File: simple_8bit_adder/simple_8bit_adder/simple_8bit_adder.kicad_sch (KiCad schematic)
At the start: 46 parts, among them Q10_0 2N7002, Q10_1 2N7002, Q11_0 2N7002, Q15_0 2N7002, Q15_1 2N7002, Q15_2 2N7002, Q15_3 2N7002, Q19_0 2N7002, Q19_1 2N7002, Q1_0 2N7002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

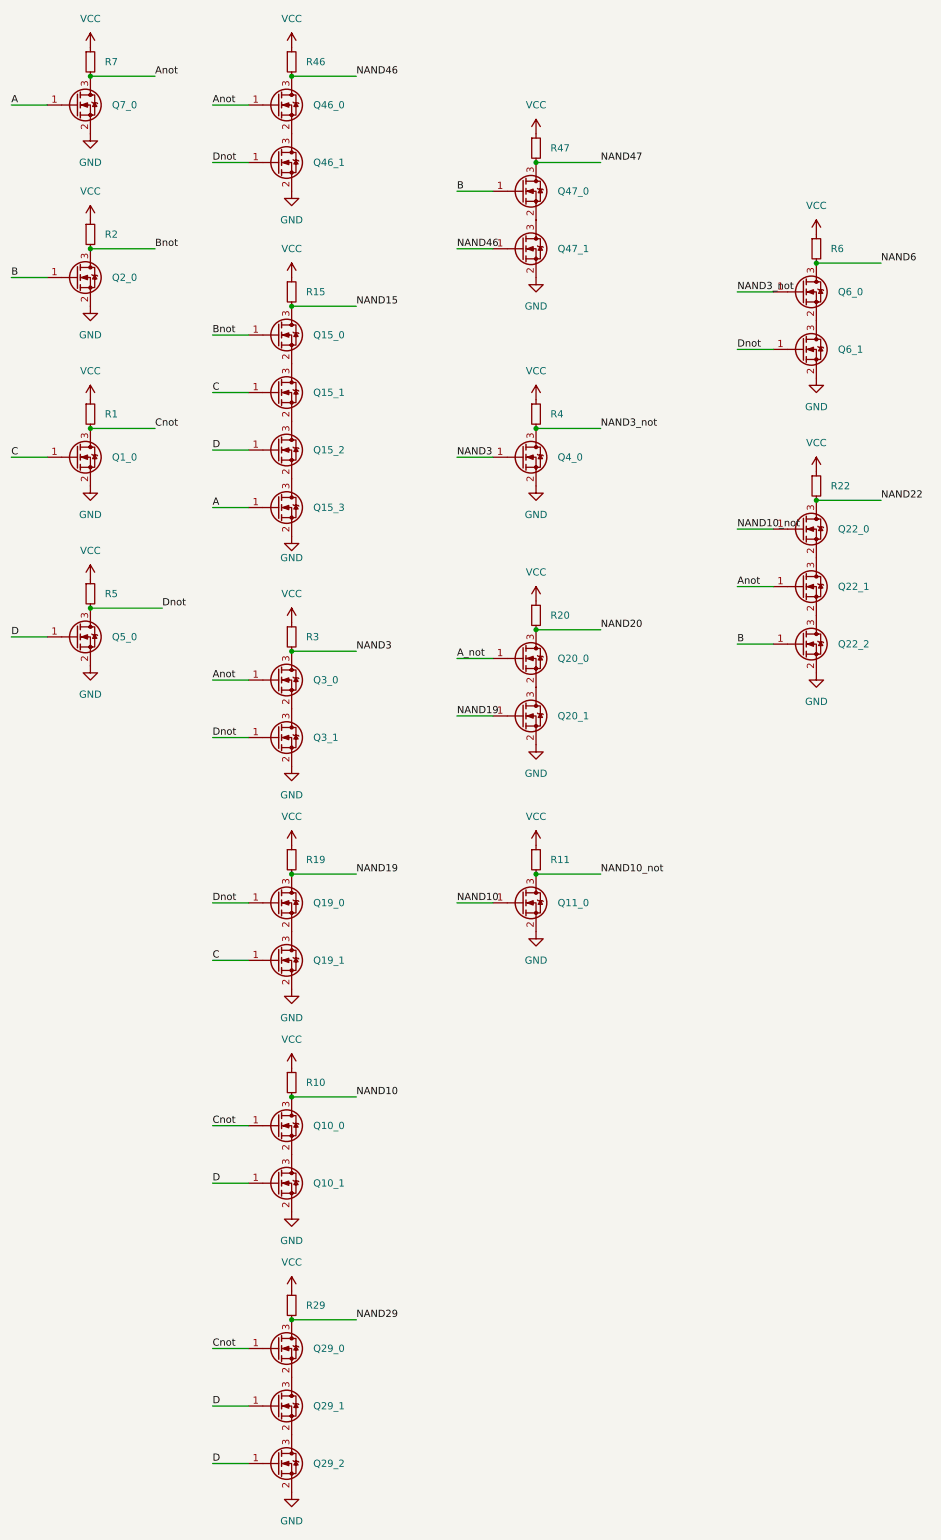
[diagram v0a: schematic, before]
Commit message: added example files
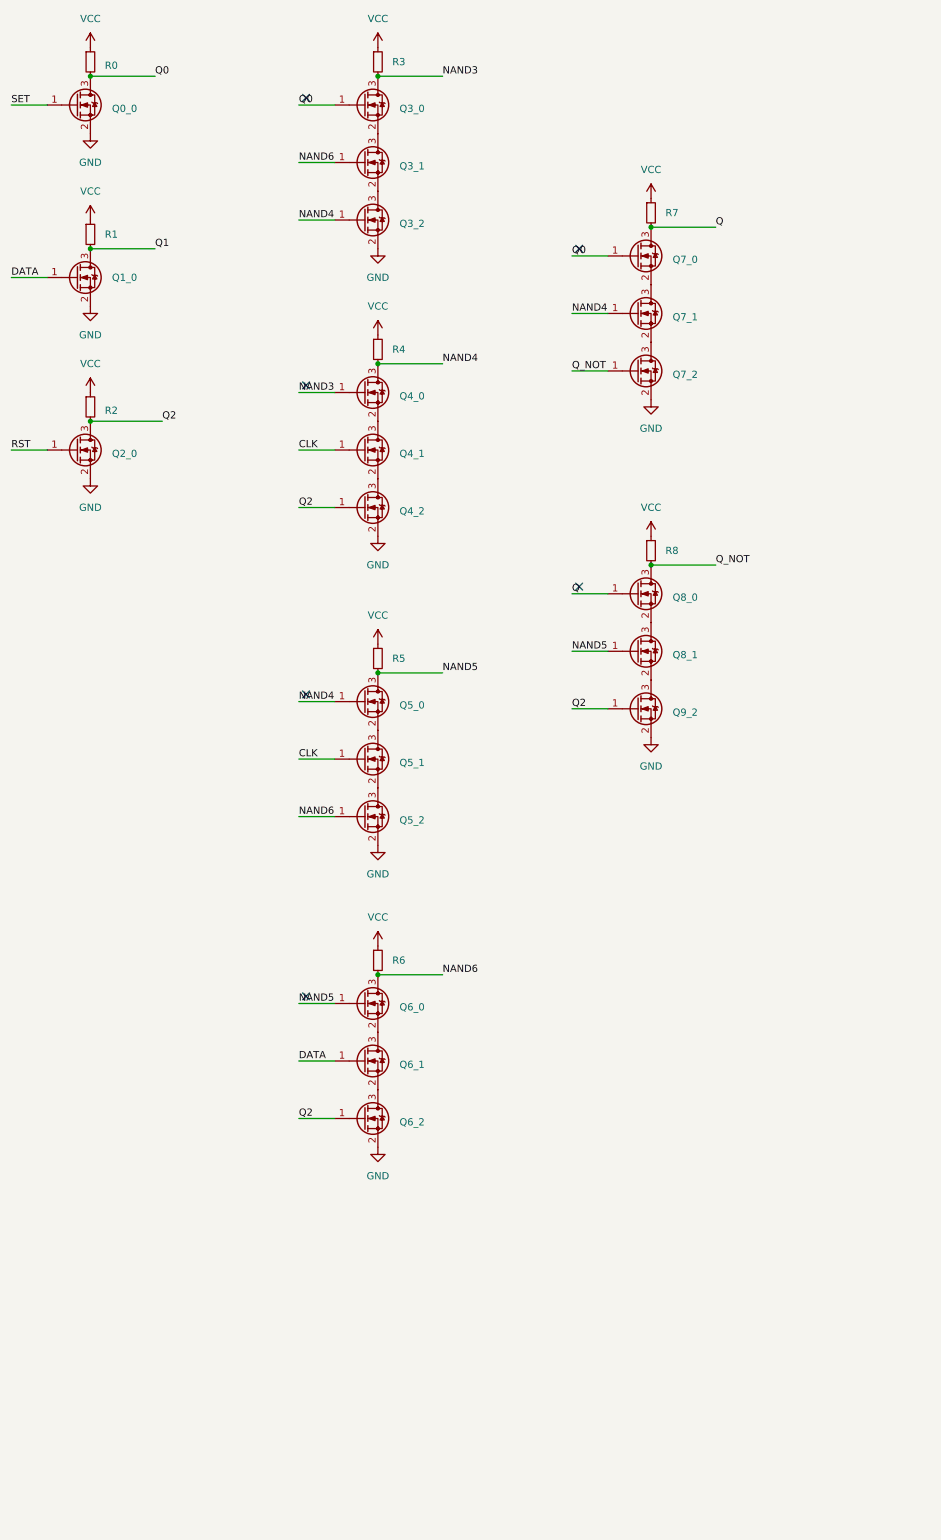
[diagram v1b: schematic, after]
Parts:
- removed Q10_0, Q10_1, Q11_0, Q15_0, Q15_1, Q15_2, Q15_3, Q19_0, Q19_1, Q20_0, Q20_1, Q22_0, Q22_1, Q22_2, Q29_0, Q29_1, Q29_2, Q2_0, Q46_0, Q46_1, Q47_0, Q47_1: 2N7002, Package_TO_SOT_SMD:SOT-23, symbol Transistor_FET:2N7002
- removed R10, R11, R15, R19, R2, R20, R22, R29, R46, R47: R_Small, Resistor_SMD:R_0402_1005Metric, symbol Device:R_Small
- added Q3_2, Q4_1, Q4_2, Q5_0, Q5_1, Q5_2, Q6_2, Q7_0, Q7_1, Q7_2, Q8_0, Q8_1, Q9_2: 2N7002, Package_TO_SOT_SMD:SOT-23, symbol Transistor_FET:2N7002
- added R5, R7, R8: R_Small, Resistor_SMD:R_0402_1005Metric, symbol Device:R_Small
- renumbered Q7_0 to Q0_0, Q5_0 to Q2_0, R7 to R0, R5 to R2
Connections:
- net GND: now also Q3_2.2 (S), Q4_2.2 (S), Q5_2.2 (S), Q6_2.2 (S), Q7_2.2 (S), Q9_2.2 (S); no longer Q3_1.2 (S), Q4_0.2 (S), Q6_1.2 (S)
- net NAND6: now also Q3_1.1 (G), Q5_2.1 (G)
- net VCC: now also R5.1, R7.1, R8.1
- net A renamed SET
- net Anot renamed Q0
- net Q0: now also Q7_0.1 (G)
- net C renamed DATA
- net DATA: now also Q6_1.1 (G)
- net Cnot renamed Q1
- net D renamed RST
- net Dnot renamed Q2
- net Q2: now also Q4_2.1 (G), Q6_2.1 (G), Q9_2.1 (G); no longer Q3_1.1 (G), Q6_1.1 (G)
- net NAND3_not renamed NAND4
- net NAND4: now also Q3_2.1 (G), Q5_0.1 (G), Q7_1.1 (G); no longer Q6_0.1 (G)
- new net: Q5_1.2 (S), Q5_2.3 (D)
- new net: Q5_0.2 (S), Q5_1.3 (D)
- new net: Q4_1.2 (S), Q4_2.3 (D)
- new net: Q4_0.2 (S), Q4_1.3 (D)
- new net: Q8_0.2 (S), Q8_1.3 (D)
- new net: Q3_1.2 (S), Q3_2.3 (D)
- new net: Q8_1.2 (S), Q9_2.3 (D)
- new net: Q6_1.2 (S), Q6_2.3 (D)
- new net: Q7_0.2 (S), Q7_1.3 (D)
- new net: Q7_1.2 (S), Q7_2.3 (D)
- new net CLK: Q4_1.1 (G), Q5_1.1 (G)
- new net NAND5: Q5_0.3 (D), Q6_0.1 (G), Q8_1.1 (G), R5.2
- new net Q: Q7_0.3 (D), Q8_0.1 (G), R7.2
- new net Q_NOT: Q7_2.1 (G), Q8_0.3 (D), R8.2
- no-connect marks 0 -> 6
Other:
- moved on the sheet: Q1_0, Q2_0, R1, R2
